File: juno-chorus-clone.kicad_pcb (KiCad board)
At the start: 2 copper layers, 149.9 x 101.6 mm, 173 parts, among them P1 15VAC_IN, P2 AUDIO_IN, P3 AUDIO_OUT_1, P4 AUDIO_OUT_1, Q1 2SC1815, Q10 2SC1815, Q11 2SA1015, Q12 2SA1015, Q13 2SC1815, Q14 2SA1015, Q15 2SA1015, Q16 2SK30, Q17 2SK30, Q18 2SA1015, Q19 2SA1015, Q2 2SC1815, Q3 2SA1015, Q4 2SA1015, Q5 2SC1815, Q6 2SC1815, Q7 2SA1015, Q8 2SA1015, Q9 2SC1815, SW1 SW_PUSH, U1 TL082, U10 TL082, U2 LM7815CT, U3 LM7915CT, U4 TL082, U5 MN3009, U6 MN3101, U7 MN3009, U8 MN3101, U9 TL082

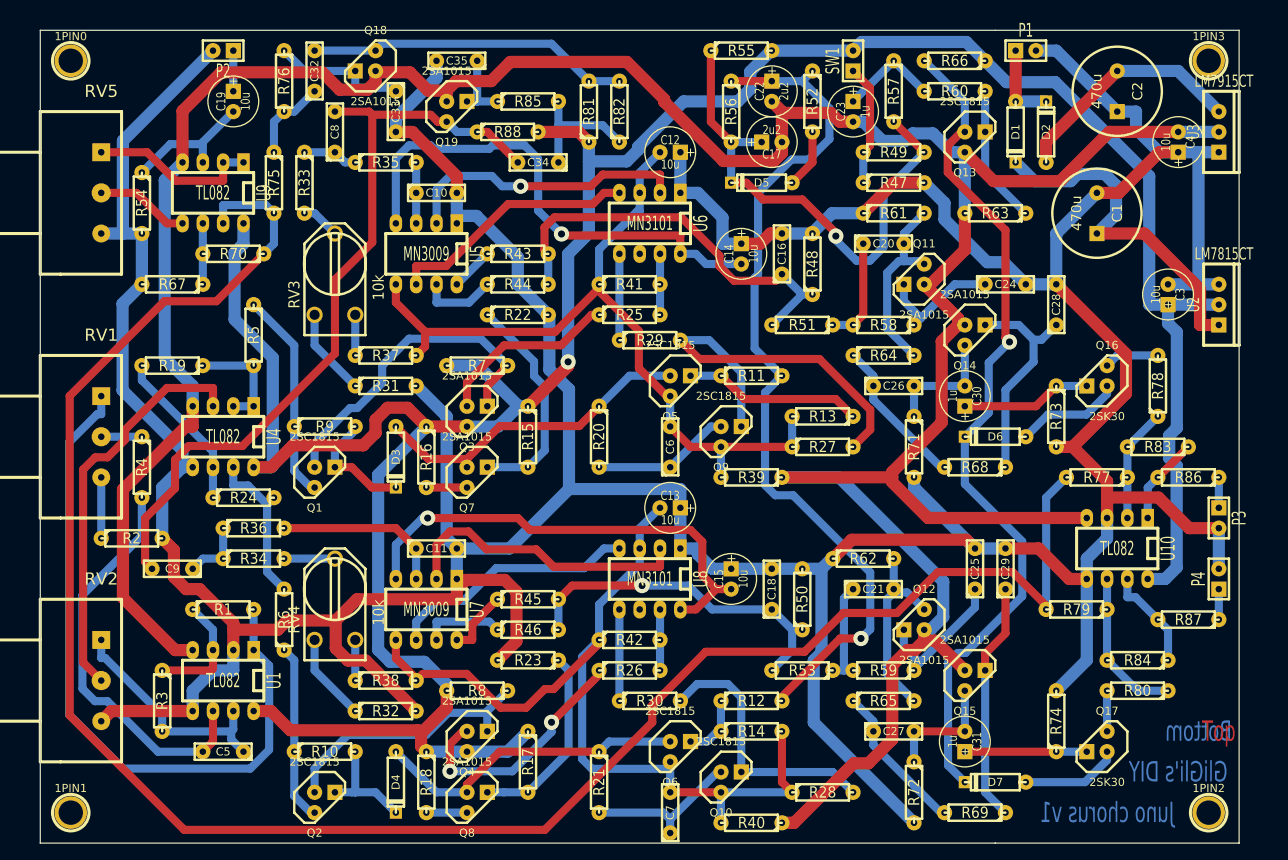
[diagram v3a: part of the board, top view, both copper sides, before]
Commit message: pcb: v2 with post-debug fixes, should be ok to build
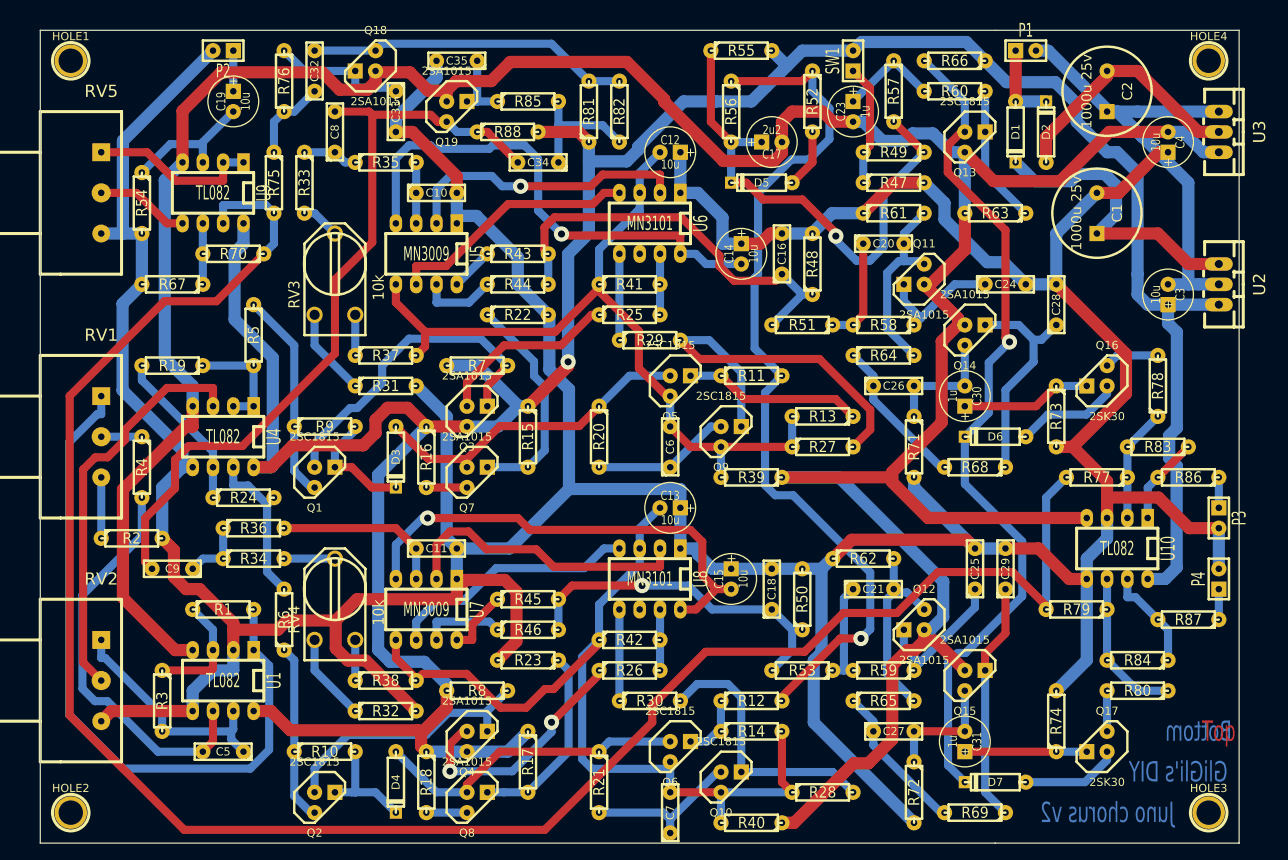
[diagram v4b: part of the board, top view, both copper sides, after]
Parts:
- removed 1PIN0: P0, 1pin
- removed 1PIN1: P1, 1pin
- removed 1PIN2: P2, 1pin
- removed 1PIN3: P3, 1pin
- removed C22: 2u2, C1V7
- added HOLE1: P***, 1pin, F.Cu at (59.7, 59.7)
- added HOLE2: P***, 1pin, F.Cu at (59.7, 153.7)
- added HOLE3: P***, 1pin, F.Cu at (201.9, 153.7)
- added HOLE4: P***, 1pin, F.Cu at (201.9, 59.7)
- C1, C2: value 470u -> 1000u 25v
- P4: value AUDIO_OUT_1 -> AUDIO_OUT_2
- R47: value 10k -> 1k
- R66: value 100k -> 10k
- R70: value 220k -> 33k
- U2, U3: footprint TO220_VERT -> TO-220_Neutral123_Vertical_LargePads
- moved U2 2.54 mm to (203.2, 87.6), turned to 270 degrees
- moved C2 1.27 mm to (189.2, 63.5)
- moved C4 1.27 mm to (196.8, 69.8)
- turned U3 to 270 degrees
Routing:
- net GND: track 652.5 -> 659.1 mm
- net N-00000104: track 44.1 -> 38.3 mm
- net VAA: track 364.1 -> 366.3 mm
- net N-00000101: track 29.9 -> 31.7 mm
- net -VAA: track 399.5 -> 398.1 mm
- net N-0000060: track 109.8 -> 110.6 mm
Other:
- board text added: "Juno chorus v2"
- board text removed: "Juno chorus v1"

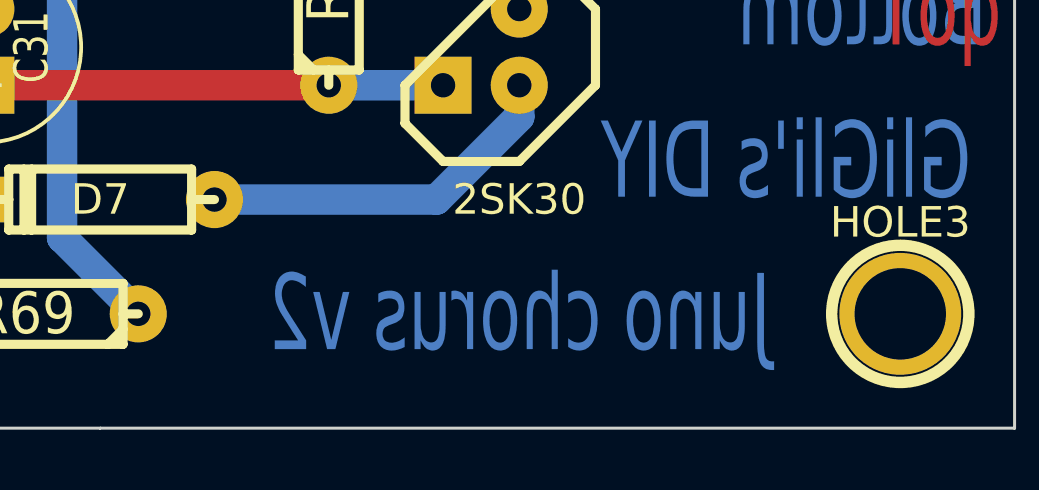
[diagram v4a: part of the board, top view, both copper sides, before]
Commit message: sch: fixing wrong res values in BBDs output stages
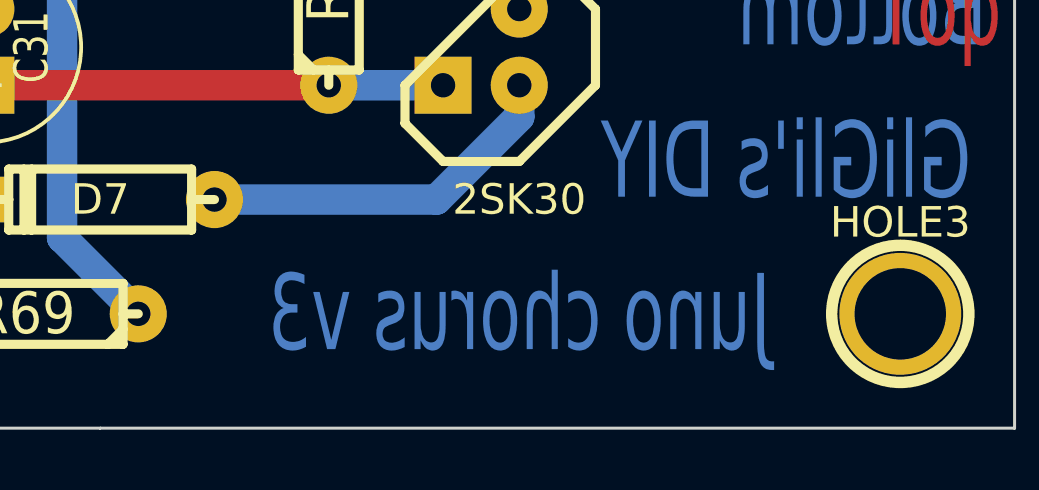
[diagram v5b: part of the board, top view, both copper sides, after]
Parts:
- R73, R74: value 10k -> 22k
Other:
- board text added: "Juno chorus v3"
- board text removed: "Juno chorus v2"
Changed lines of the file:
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@@
   (title_block
     (title "Roland Juno-60 chorus board clone")
-    (rev 2)
+    (rev 3)
     (company "GliGli's DIY")
   )
@@
       (effects (font (size 1.397 1.27) (thickness 0.2032)))
     )
-    (fp_text value 10k (at 0 0 90) (layer F.SilkS) hide
+    (fp_text value 22k (at 0 0 90) (layer F.SilkS) hide
       (effects (font (size 1.397 1.27) (thickness 0.2032)))
     )
@@
       (effects (font (size 1.397 1.27) (thickness 0.2032)))
     )
-    (fp_text value 10k (at 0 0 270) (layer F.SilkS) hide
+    (fp_text value 22k (at 0 0 270) (layer F.SilkS) hide
       (effects (font (size 1.397 1.27) (thickness 0.2032)))
     )
@@
     (effects (font (size 2.54 1.651) (thickness 0.3)) (justify mirror))
   )
-  (gr_text "Juno chorus v2" (at 189.23 153.67) (layer B.Cu)
+  (gr_text "Juno chorus v3" (at 189.23 153.67) (layer B.Cu)
     (effects (font (size 2.54 1.651) (thickness 0.3)) (justify mirror))
   )
@@
   (segment (start 71.12 143.51) (end 71.12 141.4683) (width 1.016) (layer B.Cu) (net 106))
   (segment (start 193.04 86.36) (end 193.04 73.66) (width 1.524) (layer B.Cu) (net 107))
-  (segment (start 194.31 90.17) (end 196.85 90.17) (width 1.524) (layer B.Cu) (net 107) (status 800000))
+  (segment (start 194.31 90.17) (end 196.85 90.17) (width 1.524) (layer B.Cu) (net 107))
   (segment (start 193.04 88.9) (end 194.31 90.17) (width 1.524) (layer B.Cu) (net 107))
   (segment (start 193.04 86.36) (end 193.04 88.9) (width 1.524) (layer B.Cu) (net 107))

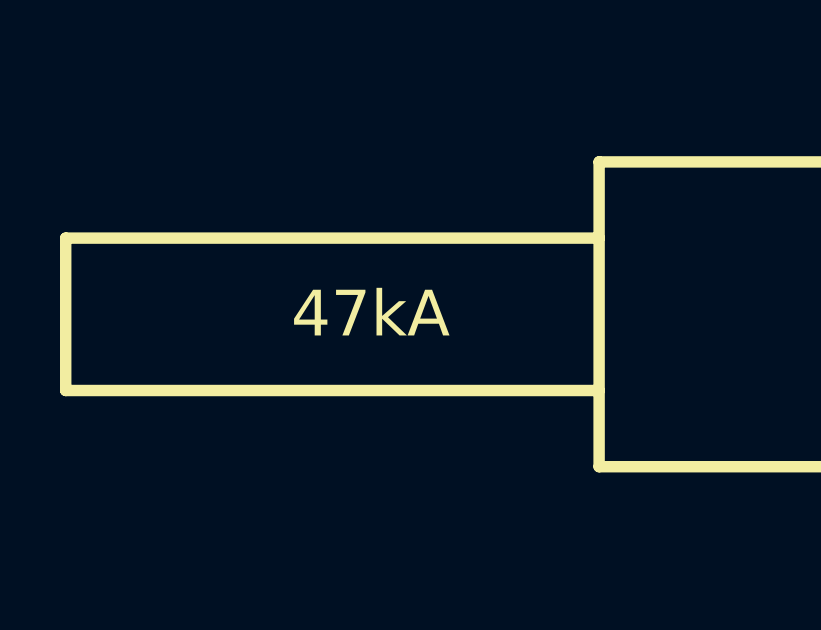
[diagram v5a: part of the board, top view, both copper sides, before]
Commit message: sch: output level / input gain pot fixes
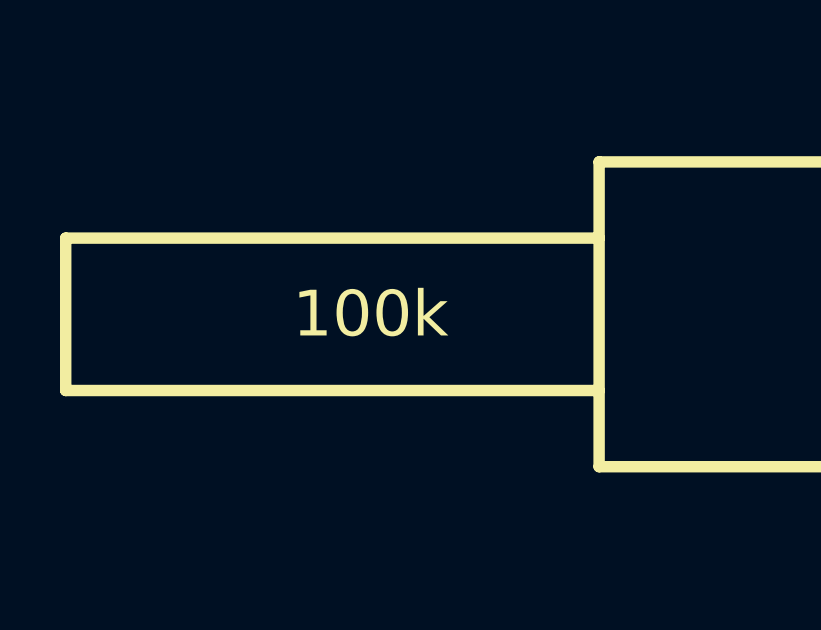
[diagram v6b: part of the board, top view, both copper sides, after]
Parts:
- R83, R84: value 4k7 -> 10k
- RV5: value 47kA -> 100k
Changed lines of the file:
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@@
     (pad_to_mask_clearance 0)
     (aux_axis_origin 55.88 55.88)
-    (visible_elements 7FFF7FFF)
+    (visible_elements 7FFFFFFF)
     (pcbplotparams
       (layerselection 270565377)
@@
       (effects (font (size 1.524 1.524) (thickness 0.3048)))
     )
-    (fp_text value 47kA (at -17.78 0) (layer F.SilkS)
+    (fp_text value 100k (at -17.78 0) (layer F.SilkS)
       (effects (font (size 1.524 1.524) (thickness 0.3048)))
     )
@@
       (effects (font (size 1.397 1.27) (thickness 0.2032)))
     )
-    (fp_text value 4k7 (at 0 0 180) (layer F.SilkS) hide
+    (fp_text value 10k (at 0 0 180) (layer F.SilkS) hide
       (effects (font (size 1.397 1.27) (thickness 0.2032)))
     )
@@
       (effects (font (size 1.397 1.27) (thickness 0.2032)))
     )
-    (fp_text value 4k7 (at 0 0 180) (layer F.SilkS) hide
+    (fp_text value 10k (at 0 0 180) (layer F.SilkS) hide
       (effects (font (size 1.397 1.27) (thickness 0.2032)))
     )
